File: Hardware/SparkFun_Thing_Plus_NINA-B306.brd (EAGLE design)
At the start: 22.9 x 66 mm, 145 parts, among them J1 USB-C, J2 THING_PLUS_LOGICAL, J3 CONN_03X2_NO4, J4 MICRO-SDFRICTION, J6 QWIIC_RA, Q1 20V/4.2A/52mΩ/1.4W, Q2 220mA/50V/3.5Ω, Q3 20V/4.2A/52mΩ/1.4W, U1 ESD Diode, U2 U-BLOX_NINA_B306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

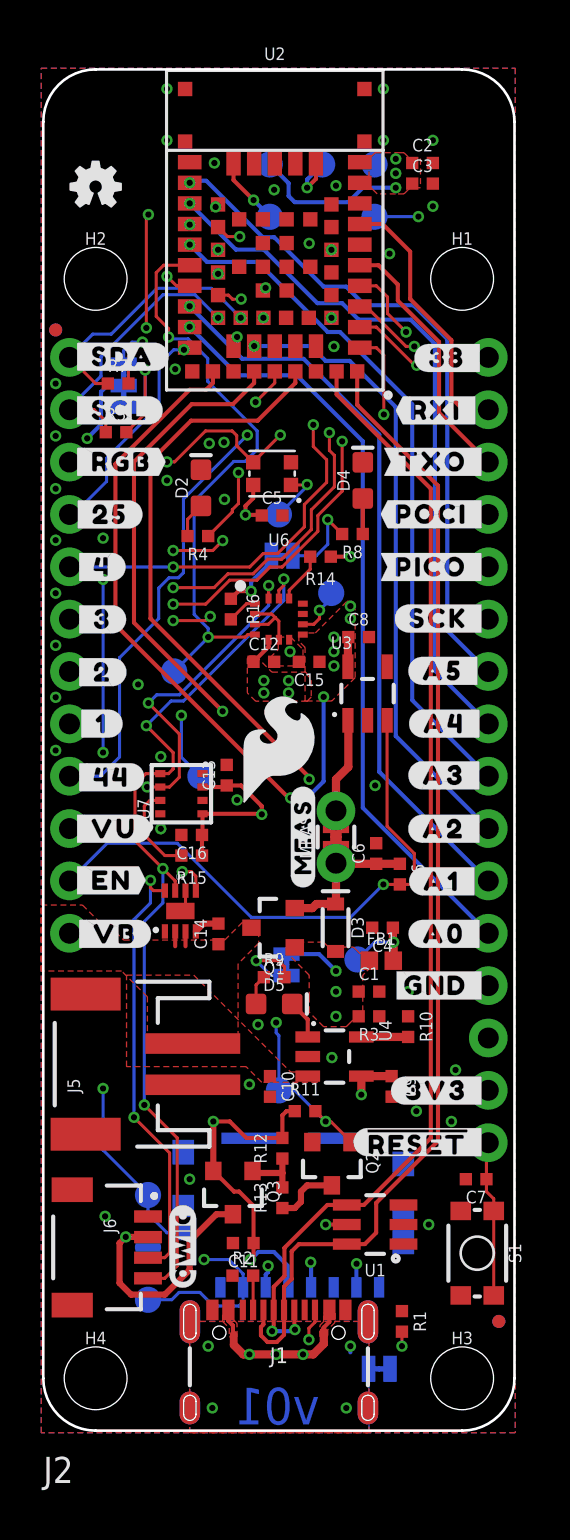
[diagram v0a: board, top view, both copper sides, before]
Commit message: v01 ready for production.
Move Power LED
Move MEAS jumper
Move GPIO6 to a new IO pin
Remove Q2
Allow ground pour between IO41 and SDA
Add vias next to BME280 ground pad
Shorten !RESET! top silk to !RST!
Swap CHG silk vertical direction
Add IMU silk from ISM BOB
Add more ground vias
Rotate !RST! on bottom silk
Reset button silk
LED silk
Add "NINA-B306" under module on top silk
Align LEDs vertically
Evenly space LEDs horizontally
Reroute
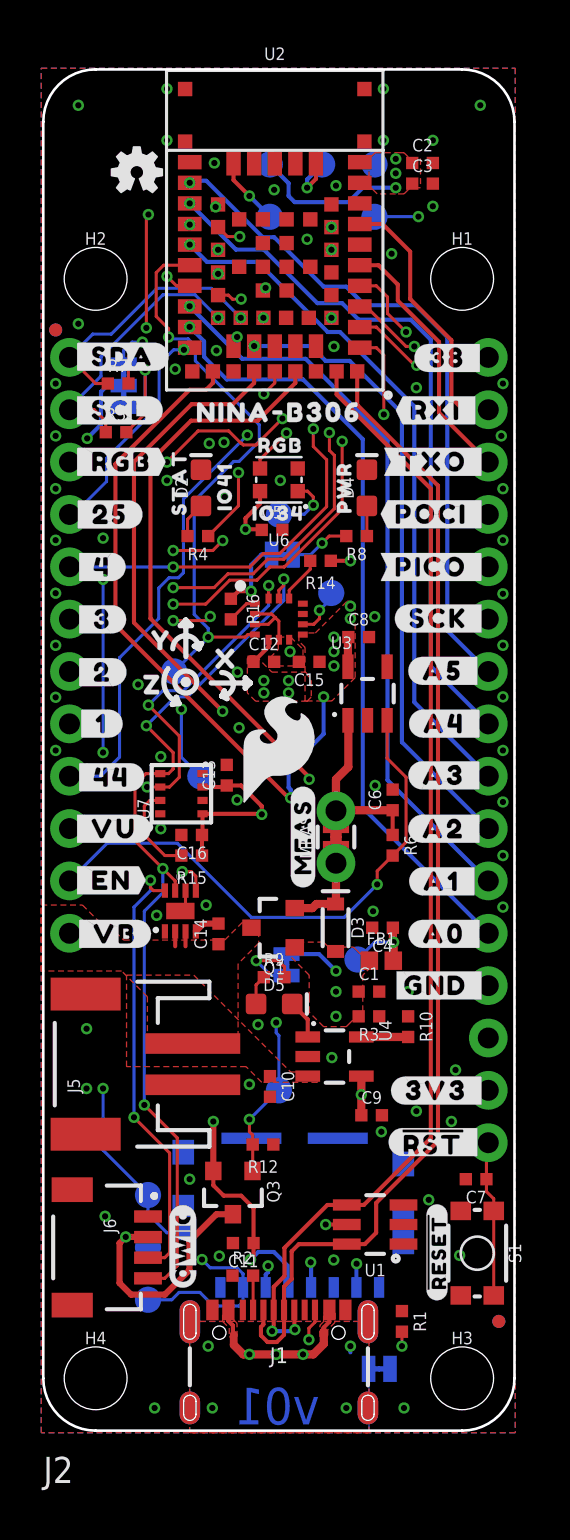
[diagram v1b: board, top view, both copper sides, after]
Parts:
- removed Q2: 220mA/50V/3.5Ω, SparkFun-DiscreteSemi:SOT23-3
- removed R11: 10k, SparkFun-Resistors:0402-TIGHT
- removed R13: 100, SparkFun-Resistors:0402-TIGHT
- added U$63: (no value), output:#_#RST##30705
- added U$64: (no value), output:RGB30710
- added U$65: (no value), output:STAT30711
- added U$66: (no value), output:PWR30712
- added U$67: (no value), output:NINA#B30630713
- added U$68: (no value), ISMTopMini:X2114
- added U$69: (no value), ISMTopMini:Y2115
- added U$70: (no value), ISMTopMini:Z2116
- added U$71: (no value), output:IO414130630715
- added U$72: (no value), output:IO34414130630716
- U$15: device output:##RESET#_#52 -> output:##RST#_#30704
- U$30: device output:#_#RST##30698 -> output:#_CHG#30707
- U$58: device output:#CHG_#92 -> output:##RESET##30708
- moved U$58 16.6 mm to (19.1, 8.65), flipped to the top, turned to 90 degrees
- moved U$30 13.6 mm to (11.8, 23.6), turned to 90 degrees
- moved C6 2.72 mm to (16.9, 30.6)
- moved LOGO5 2.12 mm to (4.54, 61.1)
- moved C9 1.70 mm to (15.9, 15.3), turned to 0 degrees
- moved R6 1.44 mm to (16.9, 28.4)
- moved R12 0.96 mm to (10.7, 13.9), turned to 180 degrees
- moved C5 0.70 mm to (11.1, 43.7)
- moved D1 0.45 mm to (11.4, 46.1)
- moved D4 0.41 mm to (15.7, 45.7)
- moved R8 0.22 mm to (15.2, 43.4)
- moved U$15 0.20 mm to (21.4, 14.0)
- moved R14 0.20 mm to (13.4, 42.2)
- moved PWR 0.05 mm to (11.6, 42.5)
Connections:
- removed net IO34/GPIO6/RGB: D1.DI, J2.3, U2.34
- removed net IO40/QWIIC_PEN: Q2.1, R11.2, TP5.1, U2.40
- removed net N$1: C6.1, D3.C, MEAS.1, MEAS.3, Q1.2, R6.1
- removed net N$13: Q2.3, R13.1
- removed net N$7: Q3.1, R12.1, R13.2
- new net IO34/RGB: D1.DI, U2.34
- new net IO35/GPIO6: J2.3, U2.35
- new net IO40/QWIIC_!PEN!: Q3.1, R12.2, TP5.1, U2.40
- new net N$12: D3.C, MEAS.1, MEAS.3, Q1.2
- net 3.3V: no longer R11.1, R12.2
- net GND: now also R12.1; no longer Q2.2
- net VIN: now also C6.1, R6.1
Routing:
- net IO40/QWIIC_PEN: track 49.5 -> 0.00 mm, vias 3 -> 0
- net IO40/QWIIC_!PEN!: track 0.00 -> 48.8 mm, vias 0 -> 3
- net IO34/GPIO6/RGB: track 22.3 -> 0.00 mm, vias 3 -> 0
- net IO35/GPIO6: track 0.00 -> 22.0 mm, vias 0 -> 3
- net IO34/RGB: track 0.00 -> 12.0 mm, vias 0 -> 2
- net N$1: track 7.93 -> 0.00 mm
- net N$12: track 0.00 -> 4.81 mm
- net 3.3V: track 45.8 -> 41.6 mm
- net VIN: track 5.41 -> 9.37 mm
- net N$13: track 3.15 -> 0.00 mm
- net N$7: track 2.89 -> 0.00 mm
- net IO22/IMU_INT2: track 30.2 -> 28.8 mm
- net EN: track 28.0 -> 26.8 mm
- net N$11: track 4.11 -> 2.95 mm
- net IO38/FREE: track 15.9 -> 16.6 mm
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
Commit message: Update for v10 post-proto changes.
Add CHG LED silk
Flip silk text direction on rear !RST!
Change GPIO6/IO35 silk
Add silk for first pin on SWD pogo
Re-place updated ESD diode.
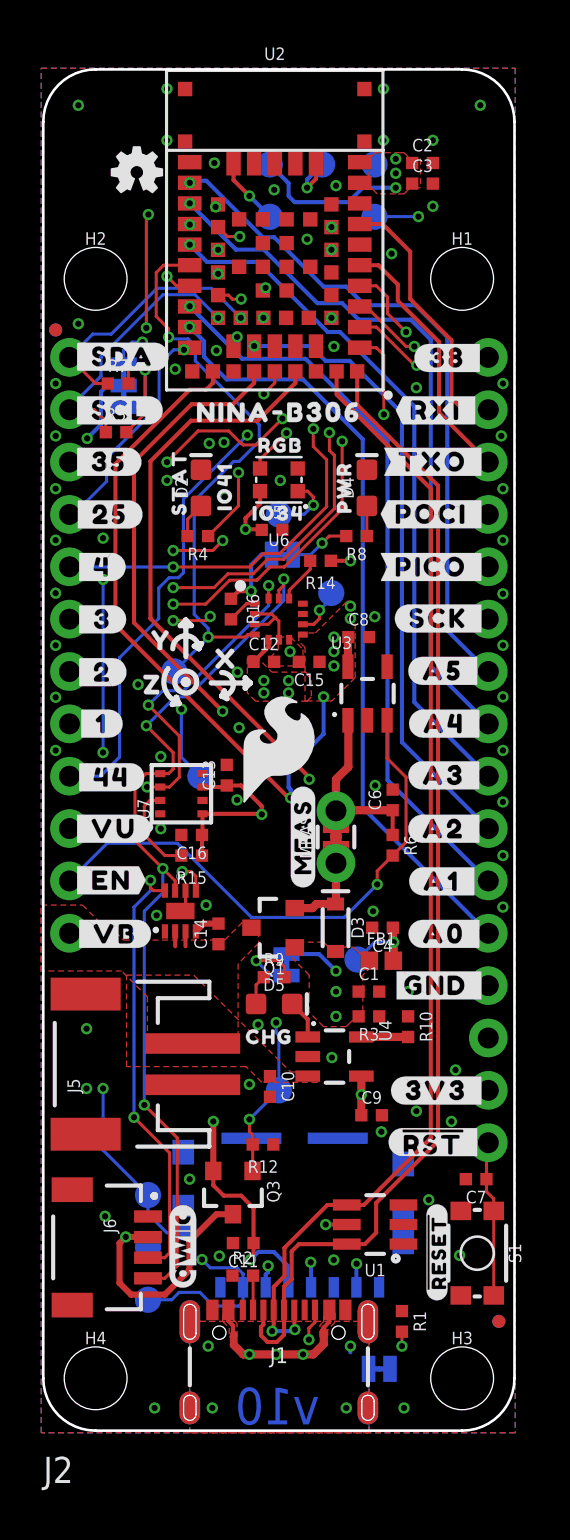
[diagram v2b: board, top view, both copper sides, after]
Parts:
- removed U$63: (no value), output:#_#RST##30705
- added U$73: (no value), output:CHG0
- added U$74: (no value), output:##RST#_#0
- U$12: device output:#_RGB#64 -> output:#_35#0
- U$45: device output:#RGB_#78 -> output:#35_#0
- moved U$45 3.50 mm to (4.80, 47.0)
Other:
- board text added: "v10"
- board text removed: "v01"
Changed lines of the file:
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@@
 <drawing>
 <settings>
-<setting alwaysvectorfont="yes"/>
+<setting alwaysvectorfont="no"/>
 <setting verticaltext="up"/>
 </settings>
@@
 <layer number="20" name="Dimension" color="24" fill="1" visible="yes" active="yes"/>
 <layer number="21" name="tPlace" color="20" fill="1" visible="yes" active="yes"/>
-<layer number="22" name="bPlace" color="14" fill="1" visible="no" active="yes"/>
+<layer number="22" name="bPlace" color="14" fill="1" visible="yes" active="yes"/>
 <layer number="23" name="tOrigins" color="15" fill="1" visible="yes" active="yes"/>
 <layer number="24" name="bOrigins" color="15" fill="1" visible="yes" active="yes"/>
@@
 <wire x1="20.32" y1="0" x2="2.54" y2="0" width="0.127" layer="20"/>
 <wire x1="2.54" y1="0" x2="0" y2="2.54" width="0.127" layer="20" curve="-90"/>
-<text x="13.4" y="0.3" size="1.778" layer="16" font="vector" ratio="15" rot="MR0">v01</text>
+<text x="13.4" y="0.3" size="1.778" layer="16" font="vector" ratio="15" rot="MR0">v10</text>
 <rectangle x1="11.65" y1="38" x2="11.75" y2="38.5" layer="41"/>
 <rectangle x1="10.14" y1="39.14" x2="10.24" y2="39.64" layer="41" rot="R90"/>
@@
 <element name="FRAME1" library="SparkFun-Aesthetics" package="CREATIVE_COMMONS" value="FRAME-LEDGER" x="63.16" y="5.63" smashed="yes">
 <attribute name="DESIGNER" value="Alex Brudner" x="63.16" y="5.63" size="1.778" layer="27" display="off"/>
-<attribute name="REV" value="v01" x="63.16" y="5.63" size="1.778" layer="27" display="off"/>
+<attribute name="REV" value="v10" x="63.16" y="5.63" size="1.778" layer="27" display="off"/>
 </element>
 <element name="J2" library="SparkFun-Boards" package="THING_PLUS" value="THING_PLUS_LOGICAL" x="0" y="0" smashed="yes">
@@
 <element name="U$24" library="output" package="#PICO_#60" value="" x="21.6" y="41.9" smashed="yes"/>
 <element name="U$25" library="output" package="#POCI_#61" value="" x="21.6" y="44.46" smashed="yes"/>
-<element name="U$12" library="output" package="#_RGB#64" value="" x="1.3" y="47" smashed="yes"/>
 <element name="U$14" library="output" package="#3V3_#65" value="" x="21.6" y="16.5" smashed="yes"/>
 <element name="U$29" library="output" package="#_SDA#68" value="" x="1.3" y="52.1" smashed="yes"/>
@@
 <element name="U$43" library="output" package="#_RXI#75" value="" x="21.4" y="49.5" smashed="yes" rot="MR0"/>
 <element name="U$44" library="output" package="#_38#76" value="" x="21.4" y="52.04" smashed="yes" rot="MR0"/>
-<element name="U$45" library="output" package="#RGB_#78" value="" x="1.3" y="47" smashed="yes" rot="MR0"/>
 <element name="U$46" library="output" package="#25_#79" value="" x="1.3" y="44.4" smashed="yes" rot="MR0"/>
 <element name="U$47" library="output" package="#4_#79" value="" x="1.4" y="41.9" smashed="yes" rot="MR0"/>
@@
 </element>
 <element name="U$15" library="output" package="##RST#_#30704" value="" x="21.4" y="14" smashed="yes"/>
-<element name="U$63" library="output" package="#_#RST##30705" value="" x="21.59" y="13.8" smashed="yes" rot="MR270"/>
 <element name="U$30" library="output" package="#_CHG#30707" value="" x="11.8" y="23.6" smashed="yes" rot="MR90"/>
 <element name="U$58" library="output" package="##RESET##30708" value="" x="19.1" y="8.65" smashed="yes" rot="R90"/>
@@
 <element name="U$71" library="output" package="IO414130630715" value="" x="8.8" y="45.8" smashed="yes" rot="R90"/>
 <element name="U$72" library="output" package="IO34414130630716" value="" x="11.4" y="44.5" smashed="yes"/>
+<element name="U$73" library="output" package="CHG0" value="" x="9.3" y="19.1" smashed="yes"/>
+<element name="U$74" library="output" package="##RST#_#0" value="" x="21.6" y="9.1" smashed="yes" rot="MR90"/>
+<element name="U$45" library="output" package="#35_#0" value="" x="4.8" y="47" smashed="yes" rot="MR0"/>
+<element name="U$12" library="output" package="#_35#0" value="" x="1.3" y="47" smashed="yes"/>
 </elements>
 <signals>

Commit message: Added Layer numbers
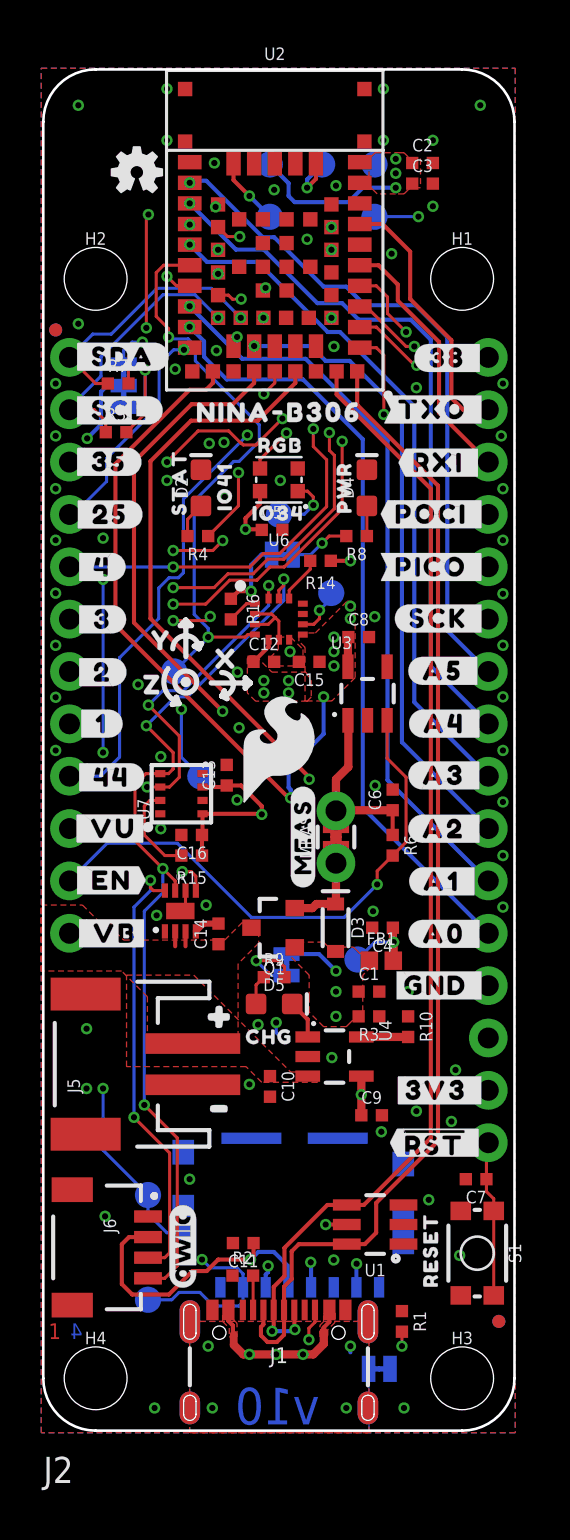
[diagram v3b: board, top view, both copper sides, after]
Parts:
- removed Q3: 20V/4.2A/52mΩ/1.4W, SparkFun-DiscreteSemi:SOT23-3
- removed R12: 10k, SparkFun-Resistors:0402-TIGHT
- removed TP5, TP6: TEST-POINT3X5, SparkFun-Connectors:PAD.03X.05
- removed U$15: (no value), output:##RST#_#30704
- added U$63: (no value), output:#_VB#0
- added U$75: (no value), output:#3
- added U$76: (no value), output:#4
- U$14: device output:#3V3_#65 -> output:RESET0
- U$3: device output:#_VB#46 -> output:#_VU#0
- U$31: device output:#_3V3#70 -> output:#_3V3#0
- U$5: device output:#_VU#48 -> output:#3V3_#0
- U$52: device output:#VUSB_#79 -> output:#VBAT_#0
- U$54: device output:#VBATT_#81 -> output:##RST#_#0
- U$58: device output:##RESET##30708 -> output:#VUSB_#0
- moved U$58 27.2 mm to (1.27, 29.2), flipped to the bottom, turned to 0 degrees
- moved U$5 23.9 mm to (21.6, 16.5)
- moved U$54 22.5 mm to (21.5, 14.0), flipped to the top
- moved U$14 8.23 mm to (18.8, 8.76), turned to 90 degrees
- moved U$3 5.11 mm to (1.27, 29.2)
- moved U$52 5.07 mm to (1.27, 24.1)
- moved U$74 4.70 mm to (21.6, 13.8)
- moved U$27 2.54 mm to (21.4, 47.0)
- moved U$43 2.54 mm to (21.5, 47.0)
- moved U$26 2.54 mm to (21.6, 49.5)
- moved U$42 2.54 mm to (21.4, 49.5)
- moved U$31 0.06 mm to (21.5, 16.5)
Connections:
- removed net 3V3_QWIIC: J6.2, Q3.3, TP6.1
- net 3.3V: now also J6.2; no longer Q3.2
- net GND: no longer R12.1
- net IO40/QWIIC_!PEN!: no longer Q3.1, R12.2, TP5.1
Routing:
- net 3V3_QWIIC: track 12.9 -> 0.00 mm, vias 1 -> 0
- net IO40/QWIIC_!PEN!: track 48.8 -> 41.6 mm, vias 3 -> 2
- net 3.3V: track 41.6 -> 44.9 mm, vias 22 -> 21
- net GND: vias 70 -> 69
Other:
- board text added: "1"
- board text added: "2"
- board text added: "3"
- board text added: "4"
